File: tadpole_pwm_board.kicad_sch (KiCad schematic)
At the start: 2 parts, among them U1 PCA9685PW, U2 ATmega328PB-A

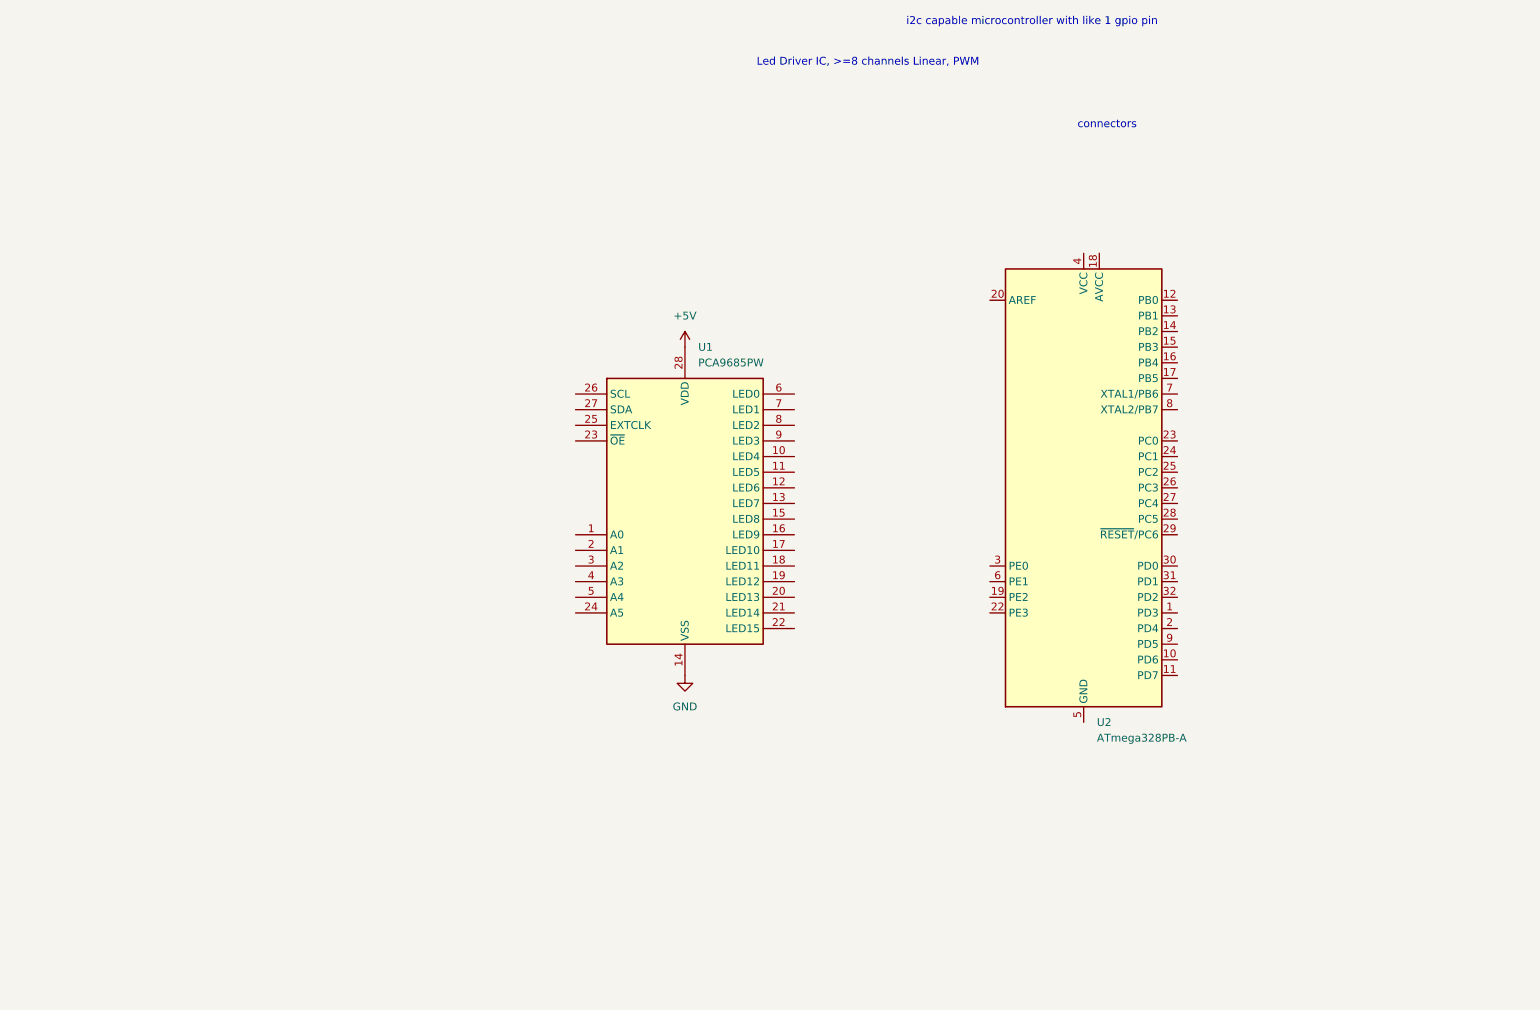
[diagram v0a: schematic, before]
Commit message: added MCU and PWM chip to schematic, as well as connectors
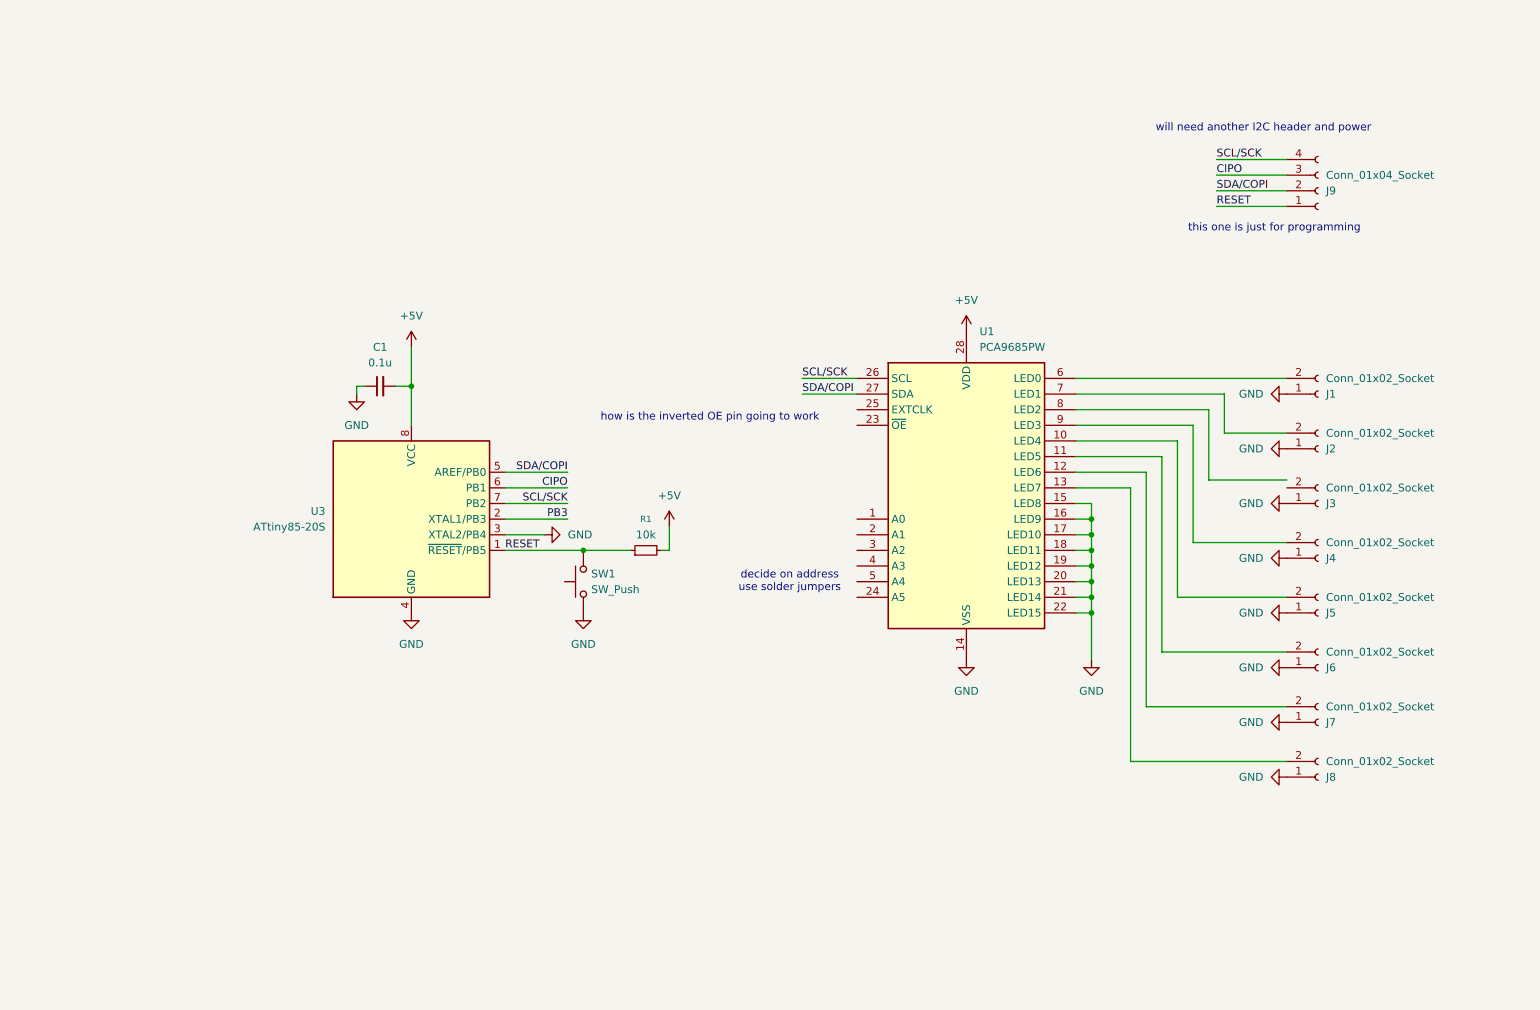
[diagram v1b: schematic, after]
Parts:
- removed U2: ATmega328PB-A, Package_QFP:TQFP-32_7x7mm_P0.8mm, symbol MCU_Microchip_ATmega:ATmega328PB-A
- added C1: 0.1u, symbol Device:C_Small
- added J1, J2, J3, J4, J5, J6, J7, J8: Conn_01x02_Socket, symbol Connector:Conn_01x02_Socket
- added J9: Conn_01x04_Socket, symbol Connector:Conn_01x04_Socket
- added R1: 10k, symbol Device:R_Small
- added SW1: SW_Push, symbol Switch:SW_Push
- added U3: ATtiny85-20S, Package_SO:SOIC-8_5.3x5.3mm_P1.27mm, symbol MCU_Microchip_ATtiny:ATtiny85-20S
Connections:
- net +5V: now also C1.2, R1.2, U3.8 (VCC)
- net GND: now also U1.15 (LED8), U1.16 (LED9), U1.17 (LED10), U1.18 (LED11), U1.19 (LED12), U1.20 (LED13), U1.21 (LED14), U1.22 (LED15), C1.1, J1.1 (Pin_1), J2.1 (Pin_1), J3.1 (Pin_1), J4.1 (Pin_1), J5.1 (Pin_1), J6.1 (Pin_1), J7.1 (Pin_1), J8.1 (Pin_1), SW1.1, U3.3 (XTAL2/PB4), U3.4 (GND)
- net at U1.10 (LED4): now also J5.2 (Pin_2)
- net at U1.11 (LED5): now also J6.2 (Pin_2)
- net at U1.12 (LED6): now also J7.2 (Pin_2)
- net at U1.13 (LED7): now also J8.2 (Pin_2)
- net SCL/SCK: now reaches U1.26 (SCL)
- net SCL/SCK: now also J9.4 (Pin_4), U3.7 (PB2)
- net SDA/COPI: now reaches U1.27 (SDA)
- net SDA/COPI: now also J9.2 (Pin_2), U3.5 (AREF/PB0)
- net at U1.6 (LED0): now also J1.2 (Pin_2)
- net at U1.7 (LED1): now also J2.2 (Pin_2)
- net at U1.9 (LED3): now also J4.2 (Pin_2)
- new net CIPO: J9.3 (Pin_3), U3.6 (PB1)
- new net PB3: U3.2 (XTAL1/PB3)
- new net RESET: J9.1 (Pin_1), R1.1, SW1.2, U3.1 (~{RESET}/PB5)
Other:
- note added: "decide on address use solder jumpers"
- note added: "how is the inverted OE pin going to work"
- note added: "this one is just for programming"
- note added: "will need another I2C header and power"
- note removed: "Led Driver IC, >=8 channels Linear, PWM"
- note removed: "connectors"
- note removed: "i2c capable microcontroller with like 1 gpio pin"
- moved on the sheet: U1

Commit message: finalized schematic, preliminary board layout
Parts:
- removed J1, J2, J3, J4, J5, J6, J7, J8: Conn_01x02_Socket, symbol Connector:Conn_01x02_Socket
- removed J9: Conn_01x04_Socket, symbol Connector:Conn_01x04_Socket
- added D1: LED, LED_SMD:LED_0805_2012Metric, symbol Device:LED
- added J1: Conn_01x10_Socket, Connector_JST:JST_XH_S10B-XH-A_1x10_P2.50mm_Horizontal, symbol Connector:Conn_01x10_Socket
- added J10, J11: Conn_01x04_Socket, Connector_JST:JST_PH_S4B-PH-K_1x04_P2.00mm_Horizontal, symbol Connector:Conn_01x04_Socket
- added J9: Conn_01x06_Socket, Connector_PinHeader_2.54mm:PinHeader_1x06_P2.54mm_Vertical, symbol Connector:Conn_01x06_Socket
- added R2, R3, R4, R5, R6, R7, R8: 10k, Resistor_SMD:R_0805_2012Metric, symbol Device:R_Small
- added R9: R_Small, Resistor_SMD:R_0805_2012Metric, symbol Device:R_Small
- added SW2: SW_DIP_x06, Button_Switch_SMD:SW_DIP_SPSTx06_Slide_6.7x16.8mm_W8.61mm_P2.54mm_LowProfile, symbol Switch:SW_DIP_x06
- C1: footprint (none) -> Capacitor_SMD:C_0805_2012Metric
- R1: footprint (none) -> Resistor_SMD:R_0805_2012Metric
- SW1: footprint (none) -> Button_Switch_SMD:SW_SPST_SKQG_WithoutStem
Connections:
- net PB3 is gone; now on net OE: U3.2 (XTAL1/PB3)
- net +5V: now also D1.2 (A), J10.3 (Pin_3), J11.3 (Pin_3), J9.5 (Pin_5), R2.1, SW2.1, SW2.2, SW2.3, SW2.4, SW2.5, SW2.6
- net CIPO: now also J9.2 (Pin_2)
- net GND: now also U1.25 (EXTCLK), J1.10 (Pin_10), J1.9 (Pin_9), J10.4 (Pin_4), J11.4 (Pin_4), J9.6 (Pin_6), R3.1, R4.1, R5.1, R6.1, R7.1, R8.1, R9.1
- net RESET: now also J9.4 (Pin_4)
- net SCL/SCK: now also J10.1 (Pin_1), J11.1 (Pin_1), J9.1 (Pin_1)
- net SDA/COPI: now also J10.2 (Pin_2), J11.2 (Pin_2), J9.3 (Pin_3)
- net PWM4: now reaches U1.9 (LED3)
- net PWM4: now also J1.4 (Pin_4)
- net A0: now reaches U1.1 (A0)
- net A0: now also R8.2, SW2.12
- net PWM5: now reaches U1.10 (LED4)
- net PWM5: now also J1.5 (Pin_5)
- net PWM6: now reaches U1.11 (LED5)
- net PWM6: now also J1.6 (Pin_6)
- net PWM7: now reaches U1.12 (LED6)
- net PWM7: now also J1.7 (Pin_7)
- net PWM8: now reaches U1.13 (LED7)
- net PWM8: now also J1.8 (Pin_8)
- net A1: now reaches U1.2 (A1)
- net A1: now also R7.2, SW2.11
- net OE: now reaches U1.23 (~{OE})
- net OE: now also R2.2
- net A5: now reaches U1.24 (A5)
- net A5: now also R3.2, SW2.7
- net A2: now reaches U1.3 (A2)
- net A2: now also R6.2, SW2.10
- net A3: now reaches U1.4 (A3)
- net A3: now also R5.2, SW2.9
- net A4: now reaches U1.5 (A4)
- net A4: now also R4.2, SW2.8
- net PWM1: now reaches U1.6 (LED0)
- net PWM1: now also J1.1 (Pin_1)
- net PWM2: now reaches U1.7 (LED1)
- net PWM2: now also J1.2 (Pin_2)
- net PWM3: now reaches U1.8 (LED2)
- net PWM3: now also J1.3 (Pin_3)
- new net: D1.1 (K), R9.2
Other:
- note added: "MCU"
- note added: "PWM Chip"
- note added: "STEMMA I2C in and out"
- note added: "programming header"
- note removed: "decide on address use solder jumpers"
- note removed: "how is the inverted OE pin going to work"
- note removed: "this one is just for programming"
- note removed: "will need another I2C header and power"
- moved on the sheet: C1, R1, SW1, U1, U3

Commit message: mounting holes, logos, labels, replaced switch
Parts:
- added H1, H2, H3, H4: MountingHole, MountingHole:MountingHole_3.2mm_M3, symbol Mechanical:MountingHole
- SW1: footprint Button_Switch_SMD:SW_SPST_SKQG_WithoutStem -> Button_Switch_SMD:SW_Push_1P1T_NO_CK_KMR2
- renumbered U3 to U2

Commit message: added PB4 Led, and labeled 5V led
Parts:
- added D2: LED, LED_SMD:LED_0805_2012Metric, symbol Device:LED
- added R10: R_Small, Resistor_SMD:R_0805_2012Metric, symbol Device:R_Small
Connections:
- net GND: now also R10.1; no longer U2.3 (XTAL2/PB4)
- new net: D2.1 (K), R10.2
- new net LED2: D2.2 (A), U2.3 (XTAL2/PB4)
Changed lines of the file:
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@@
 	(wire
 		(pts
+			(xy 110.49 66.04) (xy 110.49 83.82)
+		)
+		(stroke
+			(width 0)
+			(type default)
+		)
+	)
+	(wire
+		(pts
 			(xy 210.82 50.8) (xy 238.76 50.8)
 		)
@@
 	(wire
 		(pts
+			(xy 110.49 91.44) (xy 110.49 93.98)
+		)
+		(stroke
+			(width 0)
+			(type default)
+		)
+	)
+	(wire
+		(pts
 			(xy 140.97 102.87) (xy 146.05 102.87)
 		)
@@
 	(wire
 		(pts
+			(xy 97.79 76.2) (xy 97.79 66.04)
+		)
+		(stroke
+			(width 0)
+			(type default)
+		)
+	)
+	(wire
+		(pts
 			(xy 134.62 73.66) (xy 140.97 73.66)
 		)
@@
 	(wire
 		(pts
+			(xy 97.79 66.04) (xy 110.49 66.04)
+		)
+		(stroke
+			(width 0)
+			(type default)
+		)
+	)
+	(wire
+		(pts
 			(xy 134.62 78.74) (xy 152.4 78.74)
 		)
@@
 	(wire
 		(pts
-			(xy 77.47 76.2) (xy 83.82 76.2)
+			(xy 77.47 76.2) (xy 97.79 76.2)
 		)
 		(stroke
@@
 		)
 	)
+	(label "LED2"
+		(at 102.87 66.04 0)
+		(effects
+			(font
+				(size 1.27 1.27)
+			)
+			(justify left bottom)
+		)
+	)
 	(label "A3"
 		(at 134.62 81.28 0)
@@
 	(symbol
 		(lib_id "power:GND")
-		(at 83.82 76.2 90)
+		(at 110.49 99.06 0)
 		(unit 1)
 		(body_style 1)
@@
 		(fields_autoplaced yes)
 		(property "Reference" "#PWR07"
-			(at 90.17 76.2 0)
+			(at 110.49 105.41 0)
 			(hide yes)
 			(show_name no)
@@
 		)
 		(property "Value" "GND"
-			(at 87.63 76.1999 90)
+			(at 110.49 104.14 0)
 			(show_name no)
 			(do_not_autoplace no)
@@
 					(size 1.27 1.27)
 				)
-				(justify right)
 			)
 		)
 		(property "Footprint" ""
-			(at 83.82 76.2 0)
+			(at 110.49 99.06 0)
 			(hide yes)
 			(show_name no)
@@
 		)
 		(property "Datasheet" ""
-			(at 83.82 76.2 0)
+			(at 110.49 99.06 0)
 			(hide yes)
 			(show_name no)
@@
 		)
 		(property "Description" "Power symbol creates a global label with name \"GND\" , ground"
-			(at 83.82 76.2 0)
+			(at 110.49 99.06 0)
 			(hide yes)
 			(show_name no)
@@
 	)
 	(symbol
+		(lib_id "Device:LED")
+		(at 110.49 87.63 270)
+		(mirror x)
+		(unit 1)
+		(body_style 1)
+		(exclude_from_sim no)
+		(in_bom yes)
+		(on_board yes)
+		(in_pos_files yes)
+		(dnp no)
+		(property "Reference" "D2"
+			(at 106.68 87.9474 90)
+			(show_name no)
+			(do_not_autoplace no)
+			(effects
+				(font
+					(size 1.27 1.27)
+				)
+				(justify right)
+			)
+		)
+		(property "Value" "LED"
+			(at 106.68 90.4874 90)
+			(show_name no)
+			(do_not_autoplace no)
+			(effects
+				(font
+					(size 1.27 1.27)
+				)
+				(justify right)
+			)
+		)
+		(property "Footprint" "LED_SMD:LED_0805_2012Metric"
+			(at 110.49 87.63 0)
+			(hide yes)
+			(show_name no)
+			(do_not_autoplace no)
+			(effects
+				(font
+					(size 1.27 1.27)
+				)
+			)
+		)
+		(property "Datasheet" ""
+			(at 110.49 87.63 0)
+			(hide yes)
+			(show_name no)
+			(do_not_autoplace no)
+			(effects
+				(font
+					(size 1.27 1.27)
+				)
+			)
+		)
+		(property "Description" "Light emitting diode"
+			(at 110.49 87.63 0)
+			(hide yes)
+			(show_name no)
+			(do_not_autoplace no)
+			(effects
+				(font
+					(size 1.27 1.27)
+				)
+			)
+		)
+		(property "Sim.Pins" "1=K 2=A"
+			(at 110.49 87.63 0)
+			(hide yes)
+			(show_name no)
+			(do_not_autoplace no)
+			(effects
+				(font
+					(size 1.27 1.27)
+				)
+			)
+		)
+		(pin "2"
+		)
+		(pin "1"
+		)
+		(instances
+			(project "tadpole_pwm_board"
+				(path "/572d2eec-a6d5-42ea-947f-84884dea8527"
+					(reference "D2")
+					(unit 1)
+				)
+			)
+		)
+	)
+	(symbol
 		(lib_id "power:+5V")
 		(at 104.14 74.93 0)
@@
 					(unit 1)
 				)
+			)
+		)
+	)
+	(symbol
+		(lib_id "Device:R_Small")
+		(at 110.49 96.52 0)
+		(mirror x)
+		(unit 1)
+		(body_style 1)
+		(exclude_from_sim no)
+		(in_bom yes)
+		(on_board yes)
+		(in_pos_files yes)
+		(dnp no)
+		(property "Reference" "R10"
+			(at 107.95 95.2499 0)
+			(show_name no)
+			(do_not_autoplace no)
+			(effects
+				(font
+					(size 1.016 1.016)
+				)
+				(justify right)
+			)
+		)
+		(property "Value" "R_Small"
+			(at 107.95 97.7899 0)
+			(show_name no)
+			(do_not_autoplace no)
+			(effects
+				(font
+					(size 1.27 1.27)
+				)
+				(justify right)
+			)
+		)
+		(property "Footprint" "Resistor_SMD:R_0805_2012Metric"
+			(at 110.49 96.52 0)
+			(hide yes)
+			(show_name no)
+			(do_not_autoplace no)
+			(effects
+				(font
+					(size 1.27 1.27)
+				)
+			)
+		)
+		(property "Datasheet" ""
+			(at 110.49 96.52 0)
+			(hide yes)
+			(show_name no)
+			(do_not_autoplace no)
+			(effects
+				(font
+					(size 1.27 1.27)
+				)
+			)
+		)
+		(property "Description" "Resistor, small symbol"
+			(at 110.49 96.52 0)
+			(hide yes)
+			(show_name no)
+			(do_not_autoplace no)
+			(effects
+				(font
+					(size 1.27 1.27)
+				)
+			)
+		)
+		(pin "2"
+		)
+		(pin "1"
+		)
+		(instances
+			(project "tadpole_pwm_board"
+				(path "/572d2eec-a6d5-42ea-947f-84884dea8527"
+					(reference "R10")
+					(unit 1)
+				)

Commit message: swapped to 2x 4 pin headers
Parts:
- removed J1: Conn_01x10_Socket, Connector_JST:JST_XH_S10B-XH-A_1x10_P2.50mm_Horizontal, symbol Connector:Conn_01x10_Socket
- added J4, J5: Conn_01x04_Socket, Connector_JST:JST_XH_S4B-XH-A_1x04_P2.50mm_Horizontal, symbol Connector:Conn_01x04_Socket
- SW1: footprint Button_Switch_SMD:SW_Push_1P1T_NO_CK_KMR2 -> Button_Switch_SMD:SW_Tactile_SPST_NO_Straight_CK_PTS636Sx25SMTRLFS
- renumbered J9 to J1, J10 to J2, J11 to J3
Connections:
- net PWM1: now also J4.1 (Pin_1)
- net PWM2: now also J4.2 (Pin_2)
- net PWM3: now also J4.3 (Pin_3)
- net PWM4: now also J4.4 (Pin_4)
- net PWM5: now also J5.1 (Pin_1)
- net PWM6: now also J5.2 (Pin_2)
- net PWM7: now also J5.3 (Pin_3)
- net PWM8: now also J5.4 (Pin_4)

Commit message: added some information on the schematic
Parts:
- R10, R9: value R_Small -> R_LED
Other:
- note added: "Debug LED"
- note added: "I think the right facing one will connect to the Bar02"
- note added: "MCU programming header"
- note added: "Power LED"
- note added: "Set I2C address, might leave out of BOM and just accept default value"
- note removed: "programming header"
- moved on the sheet: J5
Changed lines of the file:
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@@
 		)
 	)
-	(text "programming header"
+	(text "MCU programming header"
 		(exclude_from_sim no)
 		(at 128.016 145.542 0)
@@
 		)
 	)
+	(text "Debug LED"
+		(exclude_from_sim no)
+		(at 117.602 92.456 0)
+		(effects
+			(font
+				(size 1.27 1.27)
+			)
+		)
+	)
 	(text "STEMMA I2C in and out"
 		(exclude_from_sim no)
@@
 		)
 	)
+	(text "Power LED"
+		(exclude_from_sim no)
+		(at 37.592 39.878 0)
+		(effects
+			(font
+				(size 1.27 1.27)
+			)
+		)
+	)
 	(text "MCU"
 		(exclude_from_sim no)
@@
 		)
 	)
+	(text "I think the right facing one will connect to the Bar02"
+		(exclude_from_sim no)
+		(at 73.152 178.308 0)
+		(effects
+			(font
+				(size 1.27 1.27)
+			)
+		)
+	)
+	(text "Set I2C address, might leave out of BOM and just accept default value"
+		(exclude_from_sim no)
+		(at 152.908 116.84 0)
+		(effects
+			(font
+				(size 1.27 1.27)
+			)
+		)
+	)
 	(junction
 		(at 157.48 81.28)
@@
 	(wire
 		(pts
-			(xy 210.82 60.96) (xy 238.76 60.96)
+			(xy 210.82 60.96) (xy 250.19 60.96)
 		)
 		(stroke
@@
 	(wire
 		(pts
-			(xy 210.82 68.58) (xy 238.76 68.58)
+			(xy 210.82 68.58) (xy 250.19 68.58)
 		)
 		(stroke
@@
 	(wire
 		(pts
-			(xy 210.82 66.04) (xy 238.76 66.04)
+			(xy 210.82 66.04) (xy 250.19 66.04)
 		)
 		(stroke
@@
 	(wire
 		(pts
-			(xy 210.82 63.5) (xy 238.76 63.5)
+			(xy 210.82 63.5) (xy 250.19 63.5)
 		)
 		(stroke
@@
 			)
 		)
-		(property "Value" "R_Small"
+		(property "Value" "R_LED"
 			(at 50.8 48.2599 0)
 			(show_name no)
@@
 			)
 		)
-		(property "Value" "R_Small"
+		(property "Value" "R_LED"
 			(at 107.95 97.7899 0)
 			(show_name no)
@@
 	(symbol
 		(lib_id "Connector:Conn_01x04_Socket")
-		(at 243.84 63.5 0)
+		(at 255.27 63.5 0)
 		(unit 1)
 		(body_style 1)
@@
 		(fields_autoplaced yes)
 		(property "Reference" "J5"
-			(at 245.11 63.4999 0)
+			(at 256.54 63.4999 0)
 			(show_name no)
 			(do_not_autoplace no)
@@
 		)
 		(property "Value" "Conn_01x04_Socket"
-			(at 245.11 66.0399 0)
+			(at 256.54 66.0399 0)
 			(show_name no)
 			(do_not_autoplace no)
@@
 		)
 		(property "Footprint" "Connector_JST:JST_XH_S4B-XH-A_1x04_P2.50mm_Horizontal"
-			(at 243.84 63.5 0)
+			(at 255.27 63.5 0)
 			(hide yes)
 			(show_name no)
@@
 		)
 		(property "Datasheet" ""
-			(at 243.84 63.5 0)
+			(at 255.27 63.5 0)
 			(hide yes)
 			(show_name no)
@@
 		)
 		(property "Description" "Generic connector, single row, 01x04, script generated"
-			(at 243.84 63.5 0)
+			(at 255.27 63.5 0)
 			(hide yes)
 			(show_name no)
@@
 					(unit 1)
 				)
-			)
-		)
-	)
-	(symbol
-		(lib_id "power:GND")
-		(at 236.22 87.63 0)
-		(unit 1)
-		(body_style 1)
-		(exclude_from_sim no)
-		(in_bom yes)
-		(on_board yes)
-		(in_pos_files yes)
-		(dnp no)
-		(fields_autoplaced yes)
-		(property "Reference" "#PWR012"
-			(at 236.22 93.98 0)
-			(hide yes)
-			(show_name no)
-			(do_not_autoplace no)
-			(effects
-				(font
-					(size 1.27 1.27)
-				)
-			)
-		)
-		(property "Value" "GND"
-			(at 238.76 88.8999 0)
-			(show_name no)
-			(do_not_autoplace no)
-			(effects
-				(font
-					(size 1.27 1.27)
-				)
-				(justify left)
-			)
-		)
-		(property "Footprint" ""
-			(at 236.22 87.63 0)
-			(hide yes)
-			(show_name no)
-			(do_not_autoplace no)
-			(effects
-				(font
-					(size 1.27 1.27)
-				)
-			)
-		)
-		(property "Datasheet" ""
-			(at 236.22 87.63 0)
-			(hide yes)
-			(show_name no)
-			(do_not_autoplace no)
-			(effects
-				(font
-					(size 1.27 1.27)
-				)
-			)
-		)
-		(property "Description" "Power symbol creates a global label with name \"GND\" , ground"
-			(at 236.22 87.63 0)
-			(hide yes)
-			(show_name no)
-			(do_not_autoplace no)
-			(effects
-				(font
-					(size 1.27 1.27)
-				)
-			)
-		)
-		(pin "1"
-		)
-		(instances
-			(project "tadpole_pwm_board"
-				(path "/572d2eec-a6d5-42ea-947f-84884dea8527"
-					(reference "#PWR012")
-					(unit 1)
-				)
